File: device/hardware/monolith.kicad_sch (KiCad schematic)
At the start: 116 parts, among them J1 CAN, J10 Conn_01x02_Pin, J11 UART, J12 DIN1/2, J13 DIN3/4, J14 Micro_SD_Card, J2 GPS, J3 I2C, J4 AIN1/2, J5 AIN3/4, J6 AIN5/6, J7 Conn_01x02_Pin, J8 Conn_01x02_Pin, J9 Conn_01x02_Pin, U1 ESP32-S3-WROOM-1-N4, U10 LMV321, U11 AMS1117-3.3, U2 MCP6002-xSN, U3 SN65HVD230, U4 TPS5430DDA, U5 MCP6002-xSN, U6 MPU-6050, U7 MCP6002-xSN, U8 AMS1117-3.3, U9 PCF8563T, Y1 FC135

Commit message: update: PCB prototype
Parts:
- removed C13, C14, C19: 47uF, Capacitor_SMD:C_1206_3216Metric, symbol Device:C_Small
- removed J9: Conn_01x02_Pin, Connector_PinHeader_2.54mm:PinHeader_1x02_P2.54mm_Vertical, symbol Connector:Conn_01x02_Pin
- removed R6: 1k, Resistor_SMD:R_0603_1608Metric, symbol Device:R_Small_US
- removed RV1, RV2, RV3, RV4: 1k, Potentiometer_THT:Potentiometer_Bourns_3266W_Vertical, symbol Device:R_Potentiometer_US
- removed TP1, TP2, TP3, TP4: TestPoint, Connector_PinHeader_2.54mm:PinHeader_1x01_P2.54mm_Vertical, symbol Connector:TestPoint
- added C16, C17: 47uF, Capacitor_SMD:C_1206_3216Metric, symbol Device:C_Small
- added C22, C28, C38: 0.1uF, Capacitor_SMD:C_0603_1608Metric, symbol Device:C_Small
- added C31, C32, C33, C34, C35, C36, C37: 22nF, Capacitor_SMD:C_0603_1608Metric, symbol Device:C_Small
- added J14: I2C2, Connector_PinHeader_1.00mm:PinHeader_1x02_P1.00mm_Vertical, symbol Connector:Conn_01x02_Pin
- added JP2, JP3, JP6, JP7: Jumper_2_Small_Open, Connector_PinHeader_2.54mm:PinHeader_1x02_P2.54mm_Vertical, symbol Jumper:Jumper_2_Small_Open
- added R11, R12, R3, R4, R8: 1k, Resistor_SMD:R_0603_1608Metric, symbol Device:R_Small_US
- added R33, R37, R38, R39: 4.7k, Resistor_SMD:R_0603_1608Metric, symbol Device:R_Small_US
- added U13, U9: ADS1115IDGS, Package_SO:TSSOP-10_3x3mm_P0.5mm, symbol Analog_ADC:ADS1115IDGS
- J1, J2, J3, J4, J5, J6: footprint Connector_Molex:Molex_Mini-Fit_Jr_5566-04A2_2x02_P4.20mm_Vertical -> Connector_Molex:Molex_Mini-Fit_Jr_5569-04A2_2x02_P4.20mm_Horizontal
- J11: renamed from J12; footprint Connector_Molex:Molex_Mini-Fit_Jr_5566-04A2_2x02_P4.20mm_Vertical -> Connector_Molex:Molex_Mini-Fit_Jr_5569-04A2_2x02_P4.20mm_Horizontal
- J12: renamed from J13; footprint Connector_Molex:Molex_Mini-Fit_Jr_5566-04A2_2x02_P4.20mm_Vertical -> Connector_Molex:Molex_Mini-Fit_Jr_5569-04A2_2x02_P4.20mm_Horizontal
- J7: value Conn_01x02_Pin -> USB; footprint Connector_PinHeader_2.54mm:PinHeader_1x02_P2.54mm_Vertical -> Connector_PinHeader_1.00mm:PinHeader_1x02_P1.00mm_Vertical
- J8: value Conn_01x02_Pin -> CAN; footprint Connector_PinHeader_2.54mm:PinHeader_1x02_P2.54mm_Vertical -> Connector_PinHeader_1.00mm:PinHeader_1x02_P1.00mm_Vertical
- J9: renamed from J10; value Conn_01x02_Pin -> I2C1; footprint Connector_PinHeader_2.54mm:PinHeader_1x02_P2.54mm_Vertical -> Connector_PinHeader_1.00mm:PinHeader_1x02_P1.00mm_Vertical
- JP1: value Jumper_2_Small_Open -> RESET; footprint Connector_PinHeader_2.54mm:PinHeader_1x02_P2.54mm_Vertical -> Connector_PinHeader_1.00mm:PinHeader_1x02_P1.00mm_Vertical
- JP4: renamed from JP2; value Jumper_2_Small_Open -> BOOT; footprint Connector_PinHeader_2.54mm:PinHeader_1x02_P2.54mm_Vertical -> Connector_PinHeader_1.00mm:PinHeader_1x02_P1.00mm_Vertical
- JP5: renamed from JP3; value Jumper_2_Small_Open -> BTN; footprint Connector_PinHeader_2.54mm:PinHeader_1x02_P2.54mm_Vertical -> Connector_PinHeader_1.00mm:PinHeader_1x02_P1.00mm_Vertical
- JP8: renamed from JP4; value Jumper_2_Small_Open -> TERMINAL
- TP1: renamed from TP5; footprint Connector_PinHeader_2.54mm:PinHeader_1x01_P2.54mm_Vertical -> Connector_PinHeader_1.00mm:PinHeader_1x01_P1.00mm_Vertical
- TP2: renamed from TP6; footprint Connector_PinHeader_2.54mm:PinHeader_1x01_P2.54mm_Vertical -> Connector_PinHeader_1.00mm:PinHeader_1x01_P1.00mm_Vertical
- renumbered C17 to C13, C18 to C14, C16 to C18, C22 to C23, C23 to C24, C24 to C25, C25 to C26, C26 to C27, C27 to C29, C28 to C30, J11 to J10, J14 to J13, JP5 to JP9, R8 to R10, R9 to R13, R10 to R14, R11 to R15, R14 to R16, R15 to R17, R12 to R18, R13 to R19, R16 to R20, R17 to R21, R21 to R22, R22 to R23, R18 to R24, R19 to R25, R20 to R26, R23 to R27, R24 to R28, R25 to R29, R26 to R30, R27 to R31, R28 to R32, R31 to R34, R29 to R35, R30 to R36, R3 to R5, R4 to R6, R5 to R7, R7 to R9, U2 to U1, U9 to U11, U11 to U12, U1 to U2, U5 to U3, U3 to U4, U4 to U5, U7 to U6, U6 to U7
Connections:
- net +3.3VA: now also C22.1, C28.1, U13.1 (ADDR), U13.8 (VDD), U9.8 (VDD)
- net +3V3: now also J2.1 (Pin_1), J3.1 (Pin_1), C38.2, R33.1, R37.2, R38.2, R39.1, R8.1
- net +5V: now also J11.2 (Pin_2), J12.2 (Pin_2), J4.2 (Pin_2), J5.2 (Pin_2), J6.2 (Pin_2), C16.1, C17.1; no longer J11.1 (Pin_1), J12.1 (Pin_1), J2.1 (Pin_1), J3.1 (Pin_1), J4.1 (Pin_1), J5.1 (Pin_1), J6.1 (Pin_1)
- net ADC1: now also C31.2, U9.4 (AIN0); no longer U2.4 (IO4)
- net ADC2: now also C32.2, U9.5 (AIN1); no longer U2.5 (IO5)
- net ADC3: now also C33.2, U9.6 (AIN2); no longer U2.6 (IO6)
- net ADC4: now also C34.2, U9.7 (AIN3); no longer U2.7 (IO7)
- net ADC5: now also C35.2, U13.4 (AIN0); no longer U2.12 (IO8)
- net ADC6: now also C36.2, U13.5 (AIN1); no longer U2.17 (IO9)
- net ADC7: now also C37.2, U13.6 (AIN2); no longer U2.18 (IO10)
- net AIN1: now also J4.4 (Pin_4); no longer J4.3 (Pin_3)
- net AIN2: now also J4.3 (Pin_3); no longer J4.4 (Pin_4)
- net AIN3: now also J5.4 (Pin_4); no longer J5.3 (Pin_3)
- net AIN4: now also J5.3 (Pin_3); no longer J5.4 (Pin_4)
- net AIN5: now also J6.4 (Pin_4); no longer J6.3 (Pin_3)
- net AIN6: now also J6.3 (Pin_3); no longer J6.4 (Pin_4)
- net CANRX: now also J8.1 (Pin_1), U2.6 (IO6); no longer U2.35 (IO42)
- net CANTX: now also J8.2 (Pin_2), U2.7 (IO7); no longer U2.34 (IO41)
- net CLK: now also U2.32 (IO39); no longer U2.31 (IO38)
- net CMD: now also U2.33 (IO40); no longer U2.30 (IO37)
- net D1: now also U2.20 (IO12); no longer U2.19 (IO11)
- net D2: now also U2.19 (IO11); no longer U2.20 (IO12)
- net D3: now also U2.18 (IO10); no longer U2.21 (IO13)
- net D4: now also U2.17 (IO9); no longer U2.22 (IO14)
- net DAT0: now also U2.31 (IO38); no longer U2.32 (IO39)
- net DAT1: now also U2.30 (IO37); no longer U2.33 (IO40)
- net DAT2: now also U2.35 (IO42); no longer U2.28 (IO35)
- net DAT3: now also U2.34 (IO41); no longer U2.29 (IO36)
- net GND: now also J11.1 (Pin_1), J12.1 (Pin_1), C16.2, C17.2, C38.1; no longer J11.2 (Pin_2), J12.2 (Pin_2), J4.2 (Pin_2), J5.2 (Pin_2), J6.2 (Pin_2)
- net GNDA: now also J4.1 (Pin_1), J5.1 (Pin_1), J6.1 (Pin_1), C22.2, C28.2, C31.1, C32.1, C33.1, C34.1, C35.1, C36.1, C37.1, R11.1, R12.1, R3.1, R4.1, U13.3 (GND), U13.7 (AIN3), U9.1 (ADDR), U9.3 (GND)
- net GPS_RX: now also U2.14 (USB_D+); no longer J7.1 (Pin_1), U2.10 (IO17)
- net GPS_TX: now also U2.13 (USB_D-); no longer J7.2 (Pin_2), U2.11 (IO18)
- net at D3.1 (K): now also R8.2
- net at C2.2, D1.1 (A1), R1.2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: now also JP2.1 (A)
- net at C8.2, D5.1 (A1), R10.2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: now also JP7.1 (A)
- net at C3.2, D2.1 (A1), R2.2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: now also JP3.1 (A)
- net at C7.2, D4.1 (A1), R9.2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: now also JP6.1 (A)
- net at U2.23 (IO21): no longer D3.2 (A)
- net I2C_SCL renamed RX
- net RX: now also U2.9 (IO16); no longer U2.8 (IO15)
- net I2C_SDA renamed TX
- net TX: now also U2.8 (IO15); no longer U2.9 (IO16)
- net SCL renamed SCL1
- net SCL1: now also R38.1, U13.10 (SCL), U9.10 (SCL); no longer U11.6 (SCL), U7.23 (SCL)
- net SDA renamed SDA1
- net SDA1: now also R39.2, U13.9 (SDA), U9.9 (SDA); no longer U11.5 (SDA), U7.24 (SDA)
- new net: JP7.2 (B), R12.2
- new net: JP3.2 (B), R4.2
- new net: J7.1 (Pin_1), U2.10 (IO17)
- new net: J7.2 (Pin_2), U2.11 (IO18)
- new net: JP2.2 (B), R3.2
- new net: D3.2 (A), U2.5 (IO5)
- new net: JP6.2 (B), R11.2
- new net SCL2: J14.2 (Pin_2), R37.1, U11.6 (SCL), U2.22 (IO14), U7.23 (SCL)
- new net SDA2: J14.1 (Pin_1), R33.2, U11.5 (SDA), U2.21 (IO13), U7.24 (SDA)
- no-connect marks 16 -> 21
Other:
- moved on the sheet: C1, C13, C14, C2, C26, C3, C4, C5, C7, C8, D1, D2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

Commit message: update: prototype PCB
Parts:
- added C19, C39: 0.1uF, Capacitor_SMD:C_0603_1608Metric, symbol Device:C_Small
- added Q1, Q2: SS8050, Package_TO_SOT_SMD:SOT-23, symbol Transistor_BJT:SS8050
- added R40, R41: 10k, Resistor_SMD:R_0603_1608Metric, symbol Device:R_Small_US
- C1: value 1uF -> 10uF; LCSC (none) -> C19702
- C10: LCSC (none) -> C1604
- C11, C18, C22, C28, C29, C38, C4: LCSC (none) -> C14663
- C12, C15, C16, C17: LCSC (none) -> C96123
- C13, C14, C2, C26, C3, C31, C32, C33, C34, C35, C36, C37, C7, C8: LCSC (none) -> C21122
- C20, C9: LCSC (none) -> C57112
- C21, C27: LCSC (none) -> C19702
- C23, C30: LCSC (none) -> C59461
- C24, C25: LCSC (none) -> C1648
- C5: value 10uF -> 1uF; LCSC (none) -> C15849
- C6: LCSC (none) -> C13585
- D1, D2, D4, D5, D7, D8, D9: value H5VL06B -> H5VLD3B; footprint Diode_SMD:D_0603_1608Metric -> Diode_SMD:D_SOD-323; LCSC (none) -> C20615805
- D10, D11, D13, D14: LCSC (none) -> C22379456
- D3: LCSC (none) -> C2286
- D6: LCSC (none) -> C8678
- J10: footprint Connector_PinHeader_2.54mm:PinHeader_1x04_P2.54mm_Vertical -> Connector_PinHeader_2.54mm:PinHeader_2x03_P2.54mm_Vertical; symbol Connector:Conn_01x04_Pin -> Connector_Generic:Conn_02x03_Odd_Even
- J13: LCSC (none) -> C393941
- JP1: value RESET -> EN
- JP5: value BTN -> RST
- JP8: value TERMINAL -> CAN 120Ω
- L1: LCSC (none) -> C177244
- R1, R10, R11, R12, R2, R22, R23, R3, R4, R8, R9: LCSC (none) -> C21190
- R13, R14, R15, R18, R20, R21, R24, R25, R5: LCSC (none) -> C25804
- R16, R17, R27, R28, R34, R6, R7: LCSC (none) -> C22775
- R19: LCSC (none) -> C22787
- R26: LCSC (none) -> C22978
- R29: LCSC (none) -> C22809
- R30: LCSC (none) -> C23170
- R31, R32, R35, R36: LCSC (none) -> C22962
- R33, R37, R38, R39: LCSC (none) -> C23162
- U1, U3, U6: LCSC (none) -> C7377
- U10: LCSC (none) -> C7972
- U11: LCSC (none) -> C7440
- U12, U8: LCSC (none) -> C6186
- U13, U9: LCSC (none) -> C37593
- U2: LCSC (none) -> C2913197
- U4: LCSC (none) -> C12084
- U5: LCSC (none) -> C9864
- U7: LCSC (none) -> C24112
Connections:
- net +3V3: now also C1.1, C4.1, JP5.2 (B), R33.2, R37.1, R38.1, R39.2; no longer C4.2, C5.2, JP5.1 (A), R33.1, R37.2, R38.2, R39.1
- net +5V: now also J11.1 (Pin_1), J12.1 (Pin_1), J4.1 (Pin_1), J5.1 (Pin_1), J6.1 (Pin_1); no longer J11.2 (Pin_2), J12.2 (Pin_2), J4.2 (Pin_2), J5.2 (Pin_2), J6.2 (Pin_2)
- net D1: now also D14.1 (K), R36.2, U2.19 (IO11); no longer D10.1 (K), R31.2, U2.20 (IO12)
- net D2: now also D13.1 (K), R35.2, U2.20 (IO12); no longer D11.1 (K), R32.2, U2.19 (IO11)
- net D3: now also D11.1 (K), R32.2, U2.21 (IO13); no longer D13.1 (K), R35.2, U2.18 (IO10)
- net D4: now also D10.1 (K), R31.2, U2.22 (IO14); no longer D14.1 (K), R36.2, U2.17 (IO9)
- net DIN1: now also J12.4 (Pin_4), R36.1; no longer J11.3 (Pin_3), R31.1
- net DIN2: now also J12.3 (Pin_3), R35.1; no longer J11.4 (Pin_4), R32.1
- net DIN3: now also J11.4 (Pin_4), R32.1; no longer J12.3 (Pin_3), R35.1
- net DIN4: now also J11.3 (Pin_3), R31.1; no longer J12.4 (Pin_4), R36.1
- net GND: now also C1.2, C4.2, C5.2, J10.2 (Pin_2), J11.2 (Pin_2), J12.2 (Pin_2), JP1.2 (B), JP4.2 (B), C19.2, C39.2; no longer C1.1, C4.1, C5.1, J10.4 (Pin_4), J11.1 (Pin_1), J12.1 (Pin_1), JP1.1 (A), JP4.1 (A)
- net GNDA: now also J4.2 (Pin_2), J5.2 (Pin_2), J6.2 (Pin_2); no longer J4.1 (Pin_1), J5.1 (Pin_1), J6.1 (Pin_1)
- net GPS_RX: now also U2.11 (IO18); no longer U2.14 (USB_D+)
- net GPS_TX: now also U2.10 (IO17); no longer U2.13 (USB_D-)
- net RX: now also J10.3 (Pin_3), U2.36 (RXD0); no longer J3.3 (Pin_3), U2.9 (IO16)
- net SCL1: now also R38.2; no longer R38.1
- net SCL2: now also R37.2, U2.18 (IO10); no longer R37.1, U2.22 (IO14)
- net SDA1: now also R39.1; no longer R39.2
- net SDA2: now also R33.1, U2.17 (IO9); no longer R33.2, U2.21 (IO13)
- net TX: now also J10.5 (Pin_5), U2.37 (TXD0); no longer J3.4 (Pin_4), U2.8 (IO15)
- net at J7.1 (Pin_1): now also U2.13 (USB_D-); no longer U2.10 (IO17)
- net at J7.2 (Pin_2): now also U2.14 (USB_D+); no longer U2.11 (IO18)
- net EN: now reaches R5.1, U2.3 (EN)
- net EN: now also C5.1, JP1.1 (A), C19.1, Q2.3 (C); no longer C1.2, JP1.2 (B)
- net at U2.23 (IO21): now also JP5.1 (A)
- net BOOT: now reaches U2.27 (IO0)
- net BOOT: now also JP4.1 (A), C39.1, Q1.3 (C); no longer JP4.2 (B)
- net at U2.38 (IO2): no longer JP5.2 (B)
- new net: Q2.1 (B), R40.2
- new net: Q1.1 (B), R41.1
- new net DBGRX: J3.3 (Pin_3), U2.9 (IO16)
- new net DBGTX: J3.4 (Pin_4), U2.8 (IO15)
- new net DTR: J10.6 (Pin_6), Q1.2 (E), R40.1
- new net RTS: J10.4 (Pin_4), Q2.2 (E), R41.2
- no-connect marks 21 -> 19
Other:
- note added: "AUTO-PROGRAM"
- moved on the sheet: C38, D10, D14, D3, J10, JP8, R13, R19, R31, R36, R8, U2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

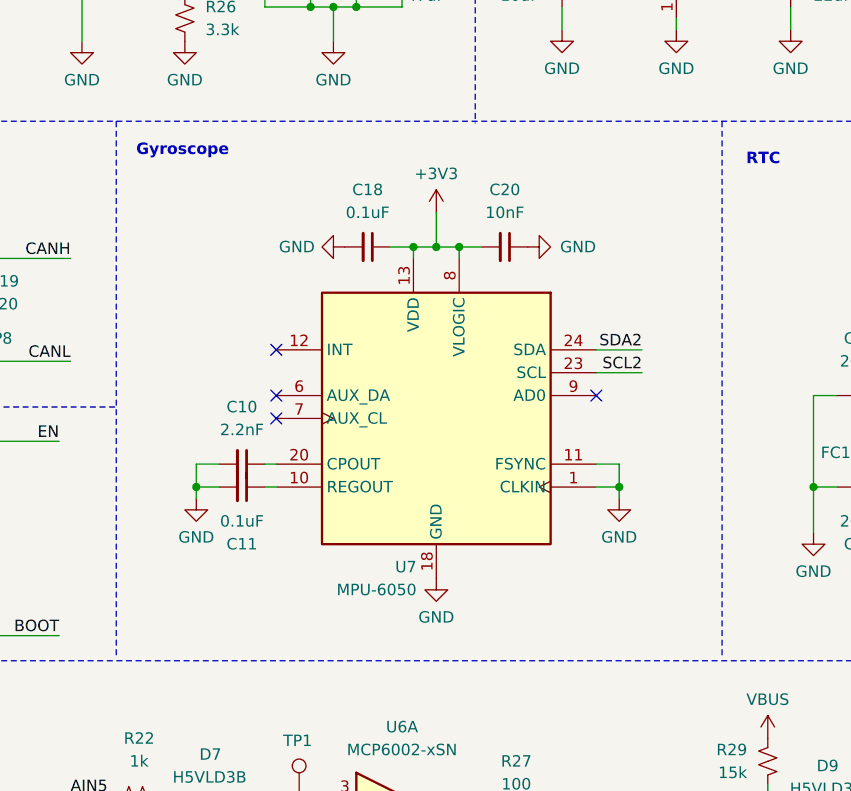
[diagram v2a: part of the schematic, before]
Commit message: update: replace MPU-6050 to MPU-6500
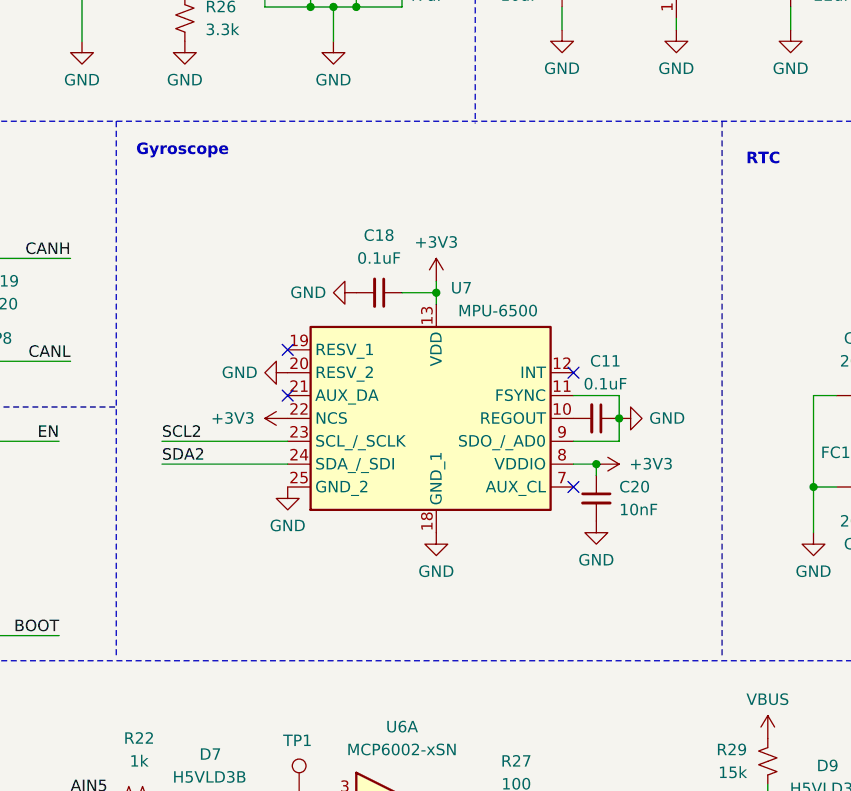
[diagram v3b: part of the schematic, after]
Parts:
- removed C10: 2.2nF, Capacitor_SMD:C_0603_1608Metric, symbol Device:C_Small
- removed U7: MPU-6050, Sensor_Motion:InvenSense_QFN-24_4x4mm_P0.5mm, symbol Sensor_Motion:MPU-6050
- added U7: MPU-6500, QFN40P300X300X95-25N-D, symbol MPU-6500:MPU-6500
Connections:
- net +3V3: now also C20.1, U7.13 (VDD), U7.22 (NCS), U7.8 (VDDIO); no longer C20.2
- net GND: now also C11.1, C20.2, U7.11 (FSYNC), U7.18 (GND_1), U7.20 (RESV_2), U7.25 (GND_2), U7.9 (SDO_/_AD0); no longer C11.2, C20.1
- net SCL2: now also U7.23 (SCL_/_SCLK)
- net SDA2: now also U7.24 (SDA_/_SDI)
- new net: C11.2, U7.10 (REGOUT)
- new net: U7.1 (NC_1), U7.14 (NC_7), U7.15 (NC_8), U7.16 (NC_9), U7.17 (NC_10), U7.2 (NC_2), U7.3 (NC_3), U7.4 (NC_4), U7.5 (NC_5), U7.6 (NC_6)

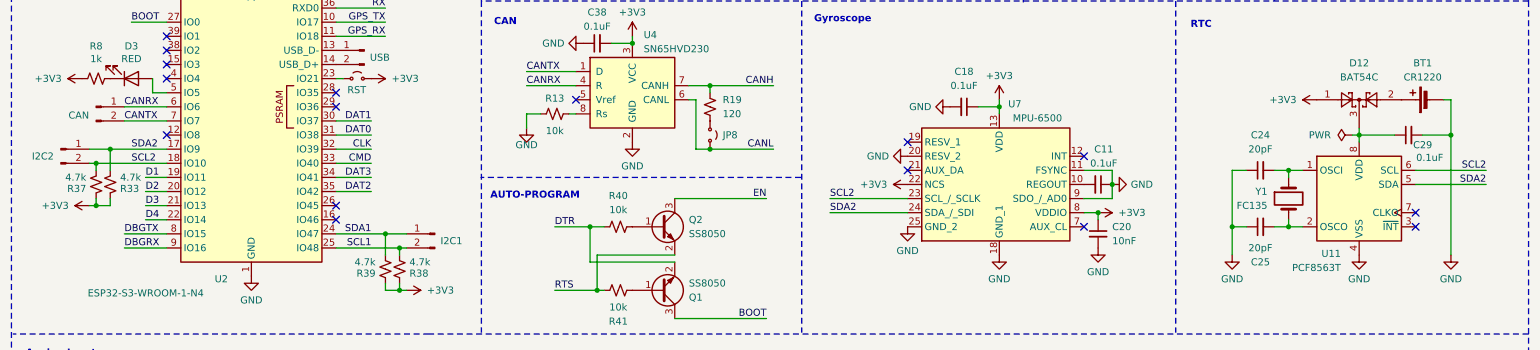
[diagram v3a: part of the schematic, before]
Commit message: update: I2C2 to I2C0
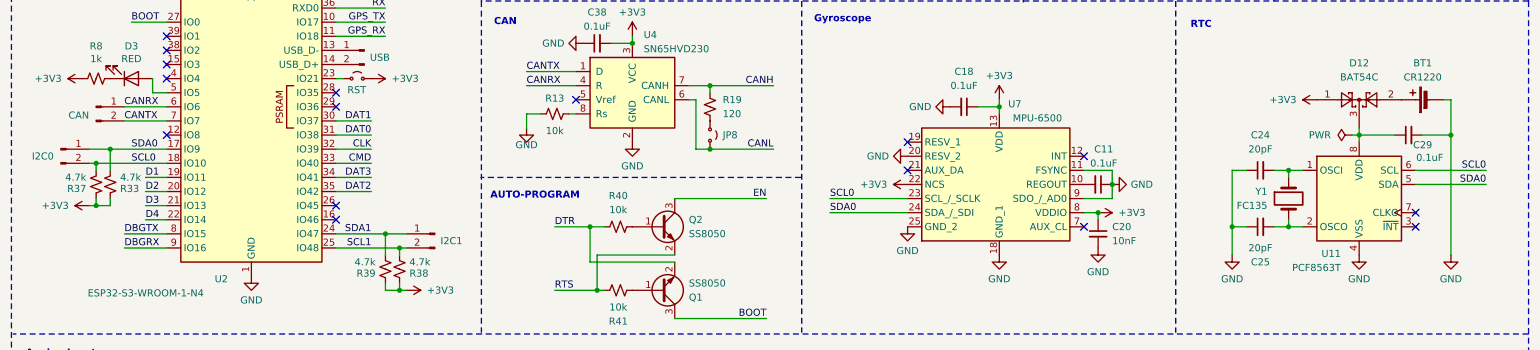
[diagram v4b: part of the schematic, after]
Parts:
- J14: value I2C2 -> I2C0
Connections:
- net SCL2 renamed SCL0
- net SDA2 renamed SDA0
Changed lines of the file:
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@@
 		)
 	)
-	(label "SCL2"
+	(label "SCL0"
 		(at 92.71 146.05 0)
 		(effects
@@
 		)
 	)
-	(label "SCL2"
+	(label "SCL0"
 		(at 218.44 152.4 0)
 		(effects
@@
 		)
 	)
-	(label "SDA2"
+	(label "SDA0"
 		(at 92.71 143.51 0)
 		(effects
@@
 		)
 	)
-	(label "SDA2"
+	(label "SDA0"
 		(at 218.44 154.94 0)
 		(effects
@@
 		)
 	)
-	(label "SCL2"
+	(label "SCL0"
 		(at 336.55 147.32 180)
 		(effects
@@
 		)
 	)
-	(label "SDA2"
+	(label "SDA0"
 		(at 336.55 149.86 180)
 		(effects
@@
 			)
 		)
-		(property "Value" "I2C2"
+		(property "Value" "I2C0"
 			(at 78.74 144.78 0)
 			(effects

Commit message: fix: wrong LED direction
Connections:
- net at R8.2: now also D3.2 (A); no longer D3.1 (K)
- net at U2.5 (IO5): now also D3.1 (K); no longer D3.2 (A)
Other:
- moved on the sheet: C19, C5, D3, J10, R5

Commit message: update: remove jumpers
PCB v2.0.1
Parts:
- removed J14: I2C0, Connector_PinHeader_1.00mm:PinHeader_1x02_P1.00mm_Vertical, symbol Connector:Conn_01x02_Pin
- removed J8: CAN, Connector_PinHeader_1.00mm:PinHeader_1x02_P1.00mm_Vertical, symbol Connector:Conn_01x02_Pin
- removed J9: I2C1, Connector_PinHeader_1.00mm:PinHeader_1x02_P1.00mm_Vertical, symbol Connector:Conn_01x02_Pin
- JP5: footprint Connector_PinHeader_1.00mm:PinHeader_1x02_P1.00mm_Vertical -> Connector_PinHeader_2.54mm:PinHeader_1x02_P2.54mm_Vertical
- U7: footprint QFN40P300X300X95-25N-D -> parts:QFN40P300X300X95-25N-D
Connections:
- net +3V3: now also R33.1, R37.2; no longer R33.2, R37.1
- net SCL0: now also R37.1; no longer R37.2
- net SDA0: now also R33.2; no longer R33.1
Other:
- moved on the sheet: R33, R37, R38, R39
